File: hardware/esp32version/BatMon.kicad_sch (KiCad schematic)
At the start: 30 parts, among them J1 Battery Connector, J2 Battery_Passthrough, J3 Conn_01x06_Pin, J4 RESET, Q1 Q_PMOS_DDGSDD_TSOP-6, Q2 Q_PMOS_DDGSDD_TSOP-6, Q3 SS8050-G, U1 ESP32-WROOM-32D, U2 LM2904, U3 AMS1117

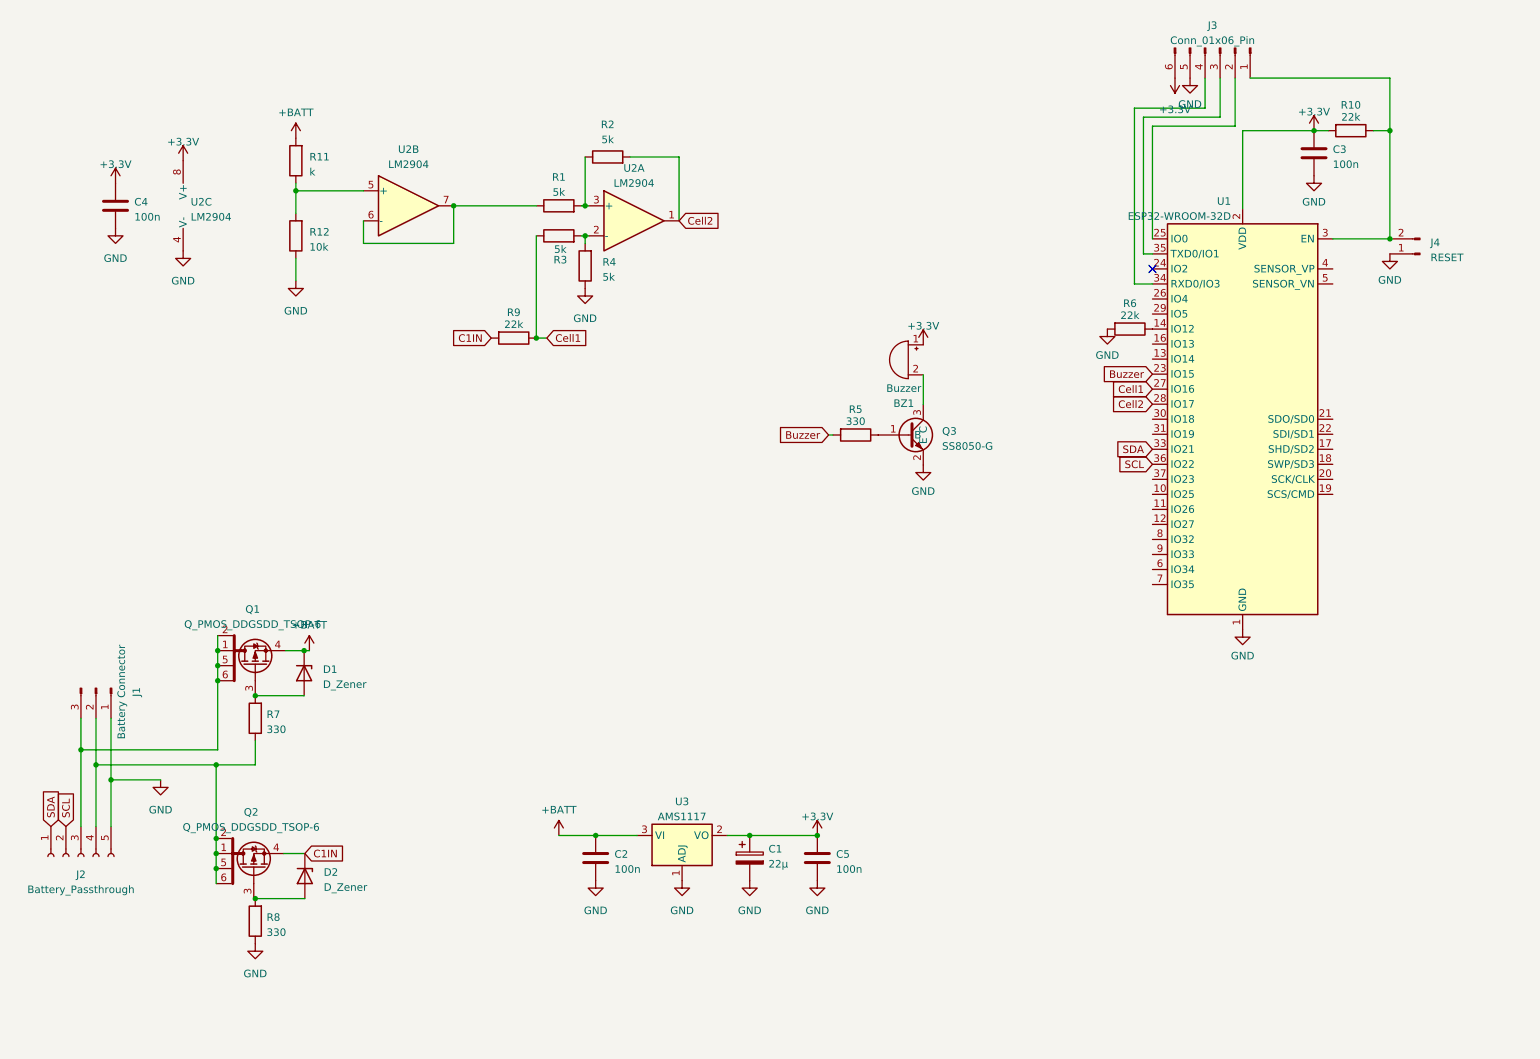
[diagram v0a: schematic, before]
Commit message: cleaned up schematic
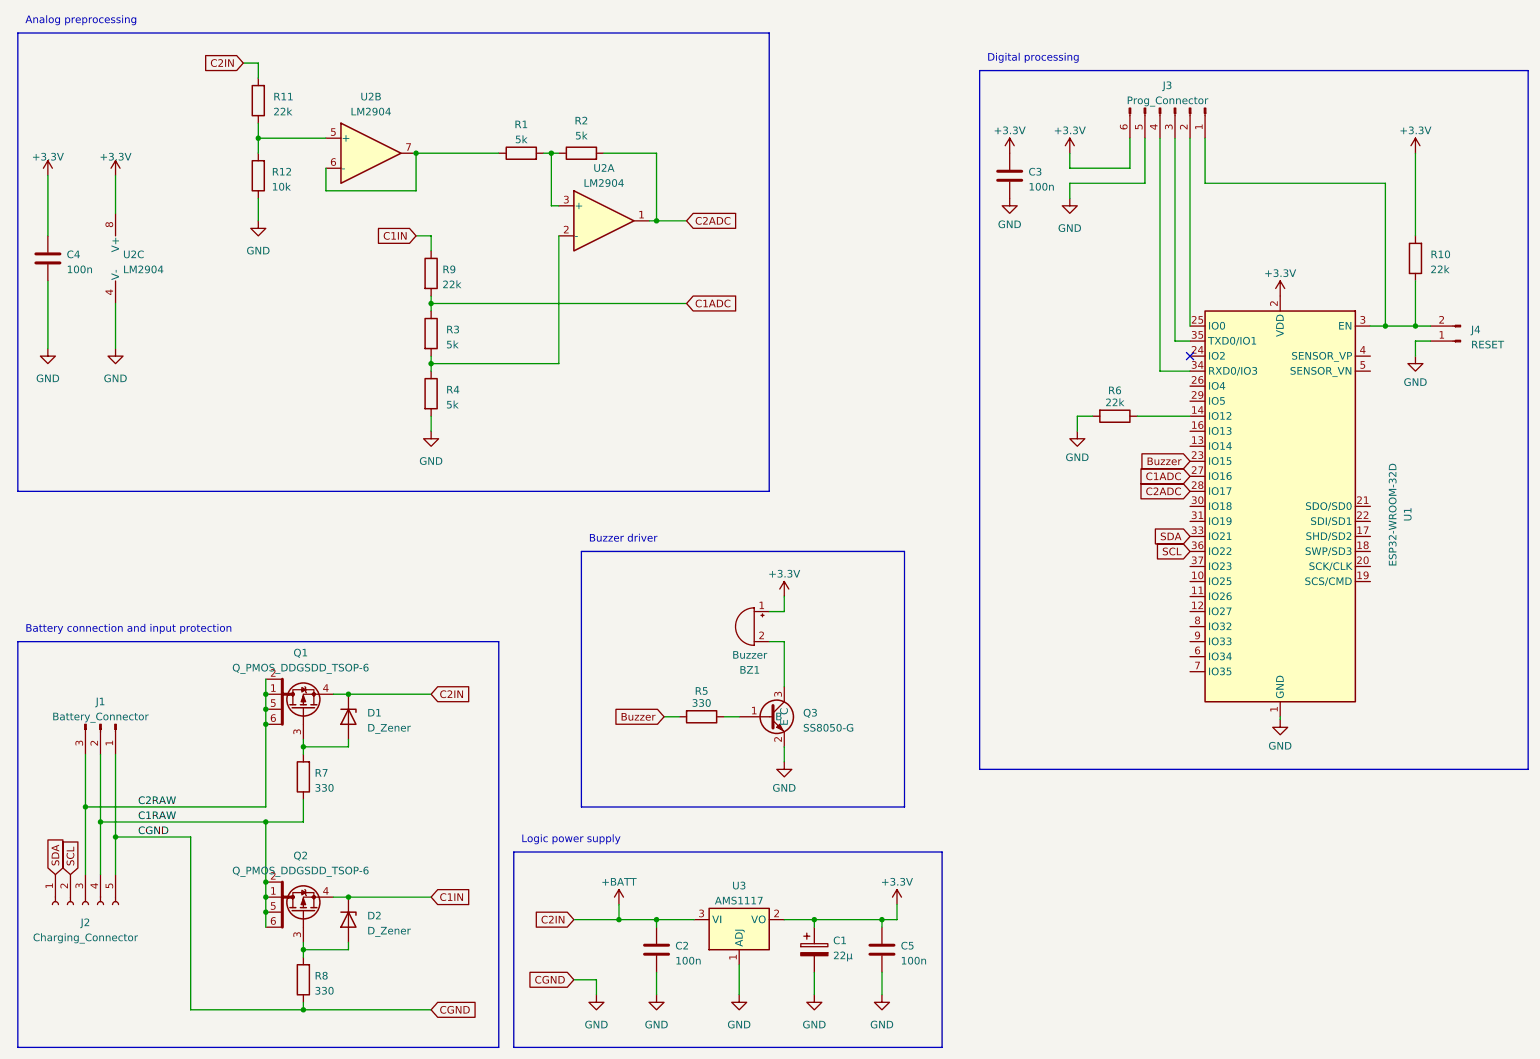
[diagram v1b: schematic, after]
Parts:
- J1: value Battery Connector -> Battery_Connector
- J2: value Battery_Passthrough -> Charging_Connector
- J3: value Conn_01x06_Pin -> Prog_Connector
- R10, R3, R9: footprint Resistor_SMD:R_0603_1608Metric_Pad0.98x0.95mm_HandSolder -> (none)
- R11: value k -> 22k
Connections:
- net C1IN: now also R9.1; no longer R9.2
- net GND: now also R4.2; no longer R4.1
- net C2RAW: now reaches J1.3 (Pin_3), J2.3 (Pin_3), Q1.1 (D), Q1.2 (D), Q1.5 (D), Q1.6 (D)
- net at R3.2, U2.2 (-): now also R4.1; no longer R4.2
- net C1RAW: now reaches J1.2 (Pin_2), J2.4 (Pin_4), Q2.1 (D), Q2.2 (D), Q2.5 (D), Q2.6 (D), R7.1
- net Cell1 renamed C1ADC
- net C1ADC: now also R9.2; no longer R9.1
- net Cell2 renamed C2ADC
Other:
- note added: "Analog preprocessing"
- note added: "Battery connection and input protection"
- note added: "Buzzer driver"
- note added: "Digital processing"
- note added: "Logic power supply"
- company: (none) -> FrenchBakery
- title: (none) -> BatMon WROOM32 Version
- moved on the sheet: BZ1, C1, C2, C3, C4, C5, D1, D2, J1, J2, J3, J4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

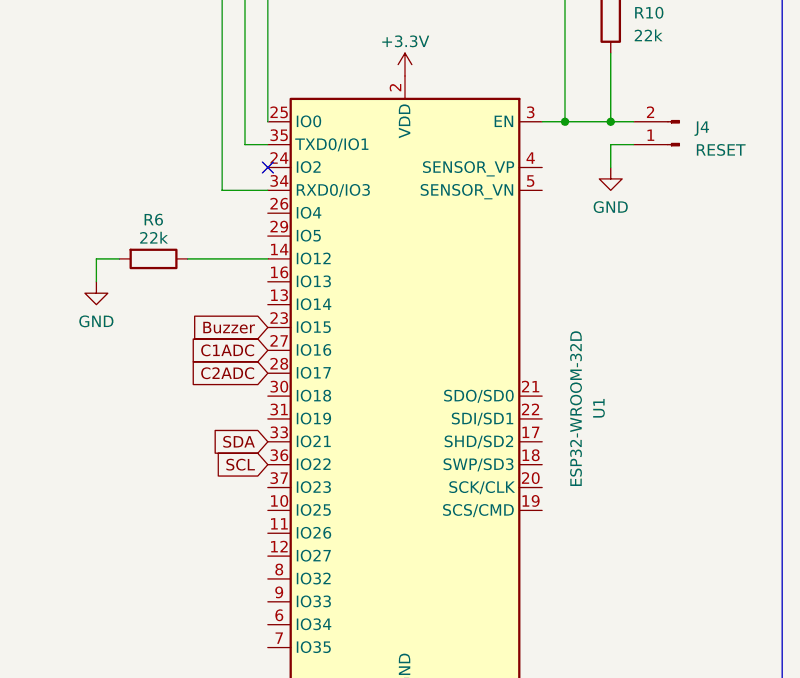
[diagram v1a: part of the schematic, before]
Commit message: added propper el_kicad_libs
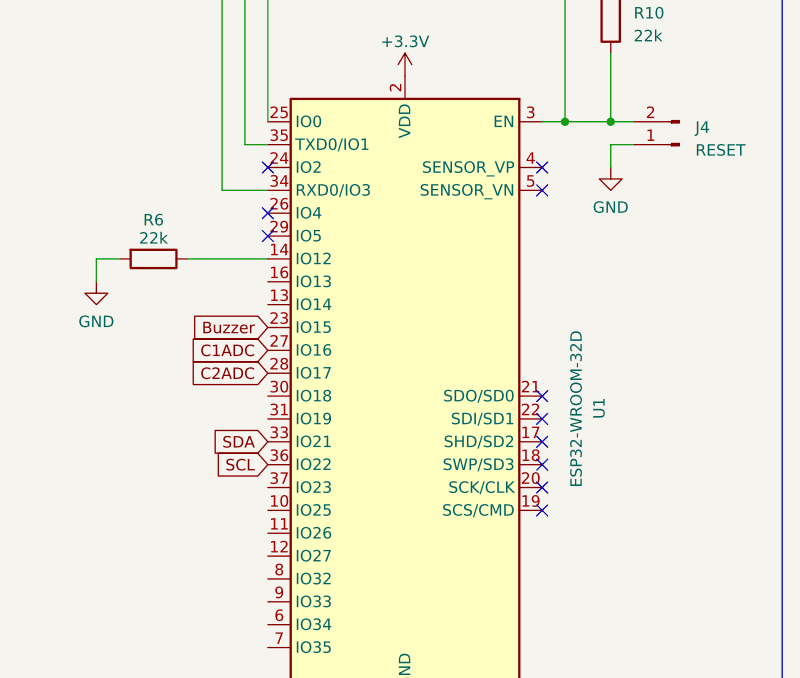
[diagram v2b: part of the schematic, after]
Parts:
- D1, D2: Mouser (none) -> https://www.mouser.at/ProductDetail/Vishay-Semiconductors/M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
- R10, R3, R9: footprint (none) -> Resistor_SMD:R_0603_1608Metric_Pad0.98x0.95mm_HandSolder
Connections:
- no-connect marks 1 -> 11
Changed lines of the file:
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@@
   (junction (at 120.65 168.91) (diameter 0) (color 0 0 0 0)
   )
+  (no_connect (at 217.17 78.74))
+  (no_connect (at 247.65 109.22))
+  (no_connect (at 217.17 81.28))
+  (no_connect (at 247.65 76.2))
+  (no_connect (at 247.65 99.06))
+  (no_connect (at 247.65 73.66))
+  (no_connect (at 247.65 106.68))
+  (no_connect (at 247.65 104.14))
+  (no_connect (at 247.65 101.6))
   (no_connect (at 217.17 73.66))
+  (no_connect (at 247.65 111.76))
   (wire (pts (xy 60.96 162.56) (xy 60.96 152.4))
     (stroke (width 0) (type default))
@@
     )
     (property "Datasheet" "~" (at 74.93 134.62 0)
+      (effects (font (size 1.27 1.27)) hide)
+    )
+    (property "Mouser" "https://www.mouser.at/ProductDetail/Vishay-Semiconductors/MMBZ4625-HE3-08?qs=ESFF34UzhwghTg091CfyaQ%3D%3D" (at 74.93 134.62 90)
       (effects (font (size 1.27 1.27)) hide)
     )
@@
       (effects (font (size 1.27 1.27)) (justify right))
     )
-    (property "Footprint" "" (at 257.048 57.15 90)
+    (property "Footprint" "Resistor_SMD:R_0603_1608Metric_Pad0.98x0.95mm_HandSolder" (at 257.048 57.15 90)
       (effects (font (size 1.27 1.27)) hide)
     )
@@
       (effects (font (size 1.27 1.27)) (justify left))
     )
-    (property "Footprint" "" (at 87.122 69.85 90)
+    (property "Footprint" "Resistor_SMD:R_0603_1608Metric_Pad0.98x0.95mm_HandSolder" (at 87.122 69.85 90)
       (effects (font (size 1.27 1.27)) hide)
     )
@@
       (effects (font (size 1.27 1.27)) (justify left))
     )
-    (property "Footprint" "" (at 87.122 59.69 90)
+    (property "Footprint" "Resistor_SMD:R_0603_1608Metric_Pad0.98x0.95mm_HandSolder" (at 87.122 59.69 90)
       (effects (font (size 1.27 1.27)) hide)
     )
@@
       (effects (font (size 1.27 1.27)) hide)
     )
+    (property "Mouser" "https://www.mouser.at/ProductDetail/Vishay-Semiconductors/MMBZ4625-HE3-08?qs=ESFF34UzhwghTg091CfyaQ%3D%3D" (at 74.93 168.91 90)
+      (effects (font (size 1.27 1.27)) hide)
+    )

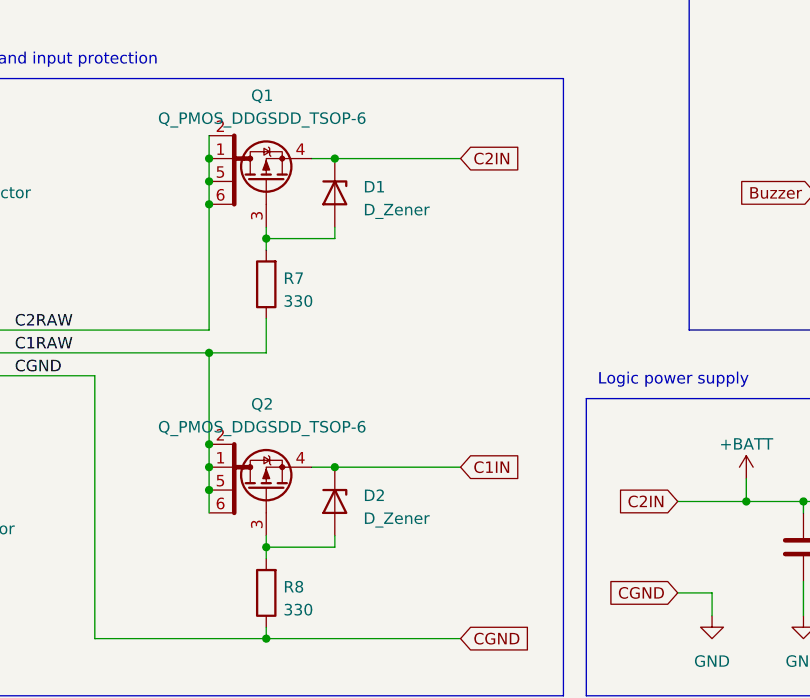
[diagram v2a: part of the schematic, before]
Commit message: reverse polarity zeners now correct pinout
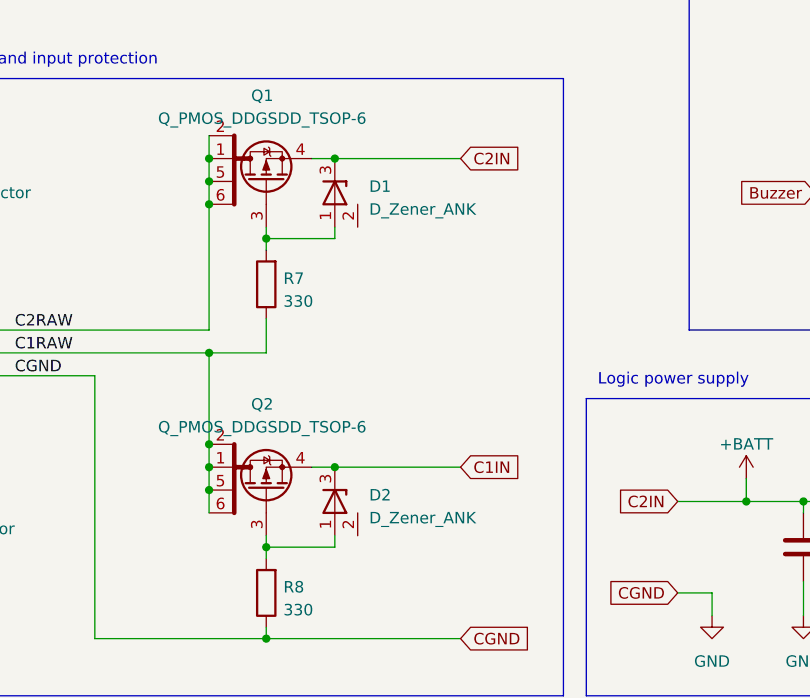
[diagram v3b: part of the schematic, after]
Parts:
- removed D1, D2: D_Zener, Package_TO_SOT_SMD:TSOT-23_HandSoldering, symbol Device:D_Zener
- added D1, D2: D_Zener_ANK, Package_TO_SOT_SMD:TSOT-23_HandSoldering, symbol ELEKTRON_Components:D_Zener_ANK
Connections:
- net +BATT: now also D1.3 (K)
- net C1IN: now also D2.3 (K)
- net at Q1.3 (G), R7.2: now also D1.1 (A)
- net at Q2.3 (G), R8.2: now also D2.1 (A)

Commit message: updated PCB
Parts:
- U1: Mouser (none) -> https://www.mouser.at/ProductDetail/Espressif-Systems/ESP32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
- U2: Mouser (none) -> https://www.mouser.at/ProductDetail/Texas-Instruments/LM290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
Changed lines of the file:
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@@
+      (effects (font (size 1.27 1.27)) hide)
+    )
+    (property "Mouser" "https://www.mouser.at/ProductDetail/Texas-Instruments/LM2904BIDR?qs=9r4v7xj2LnnFewvbXZMeJA%3D%3D" (at 78.74 39.37 0)
       (effects (font (size 1.27 1.27)) hide)
     )
@@
       (effects (font (size 1.27 1.27)) hide)
     )
+    (property "Mouser" "https://www.mouser.at/ProductDetail/Texas-Instruments/LM2904BIDR?qs=9r4v7xj2LnnFewvbXZMeJA%3D%3D" (at 118.11 50.8 0)
+      (effects (font (size 1.27 1.27)) hide)
+    )
     (pin "1")
     (pin "2")
@@
       (effects (font (size 1.27 1.27)) hide)
     )
+    (property "Mouser" "https://www.mouser.at/ProductDetail/Texas-Instruments/LM2904BIDR?qs=9r4v7xj2LnnFewvbXZMeJA%3D%3D" (at 38.1 57.15 0)
+      (effects (font (size 1.27 1.27)) hide)
+    )
     (pin "1")
     (pin "2")
@@
       (effects (font (size 1.27 1.27)) hide)
     )
+    (property "Mouser" "https://www.mouser.at/ProductDetail/Espressif-Systems/ESP32-WROOM-32E-N4?qs=Li%252BoUPsLEnsPzTWsi%252BRMgQ%3D%3D" (at 232.41 99.06 90)
+      (effects (font (size 1.27 1.27)) hide)
+    )
